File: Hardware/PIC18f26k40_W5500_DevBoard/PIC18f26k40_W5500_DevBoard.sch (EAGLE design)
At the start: 46 parts, among them J2 MAGJACK, J6 USB-B, U1 W5500, U2 PIC18F2523-I/SO

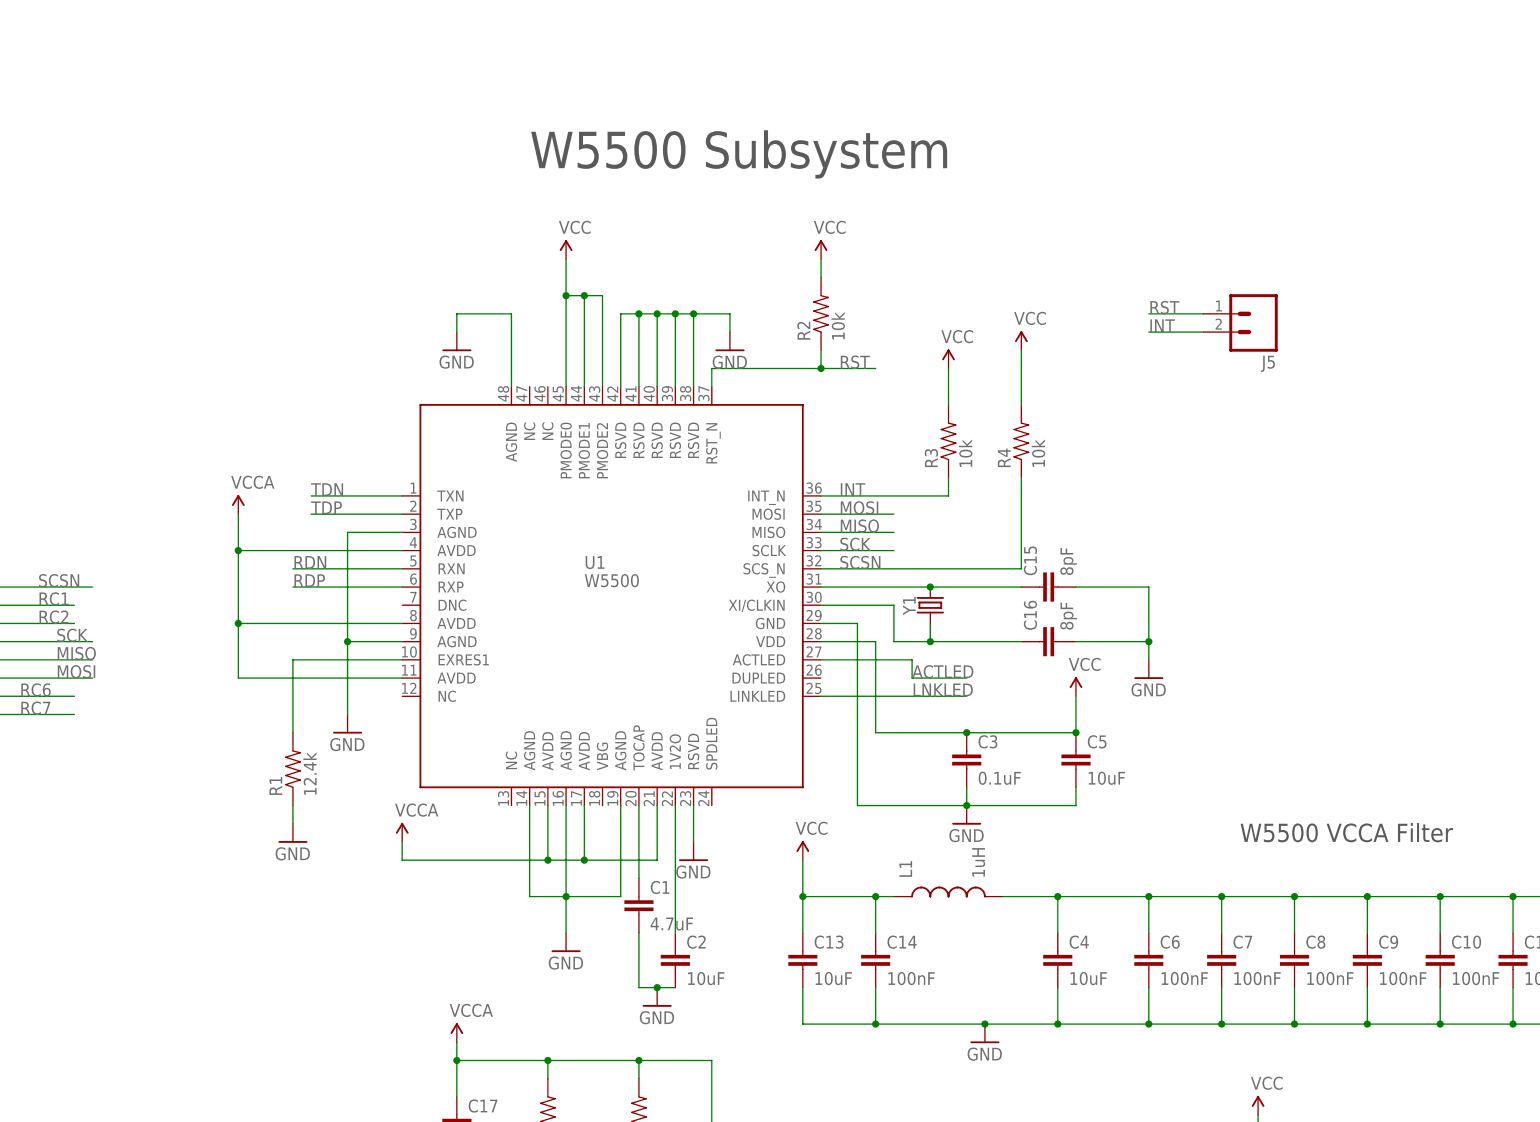
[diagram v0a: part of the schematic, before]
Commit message: #302 Added pull up and pull down resistors to Wiznet direction connections
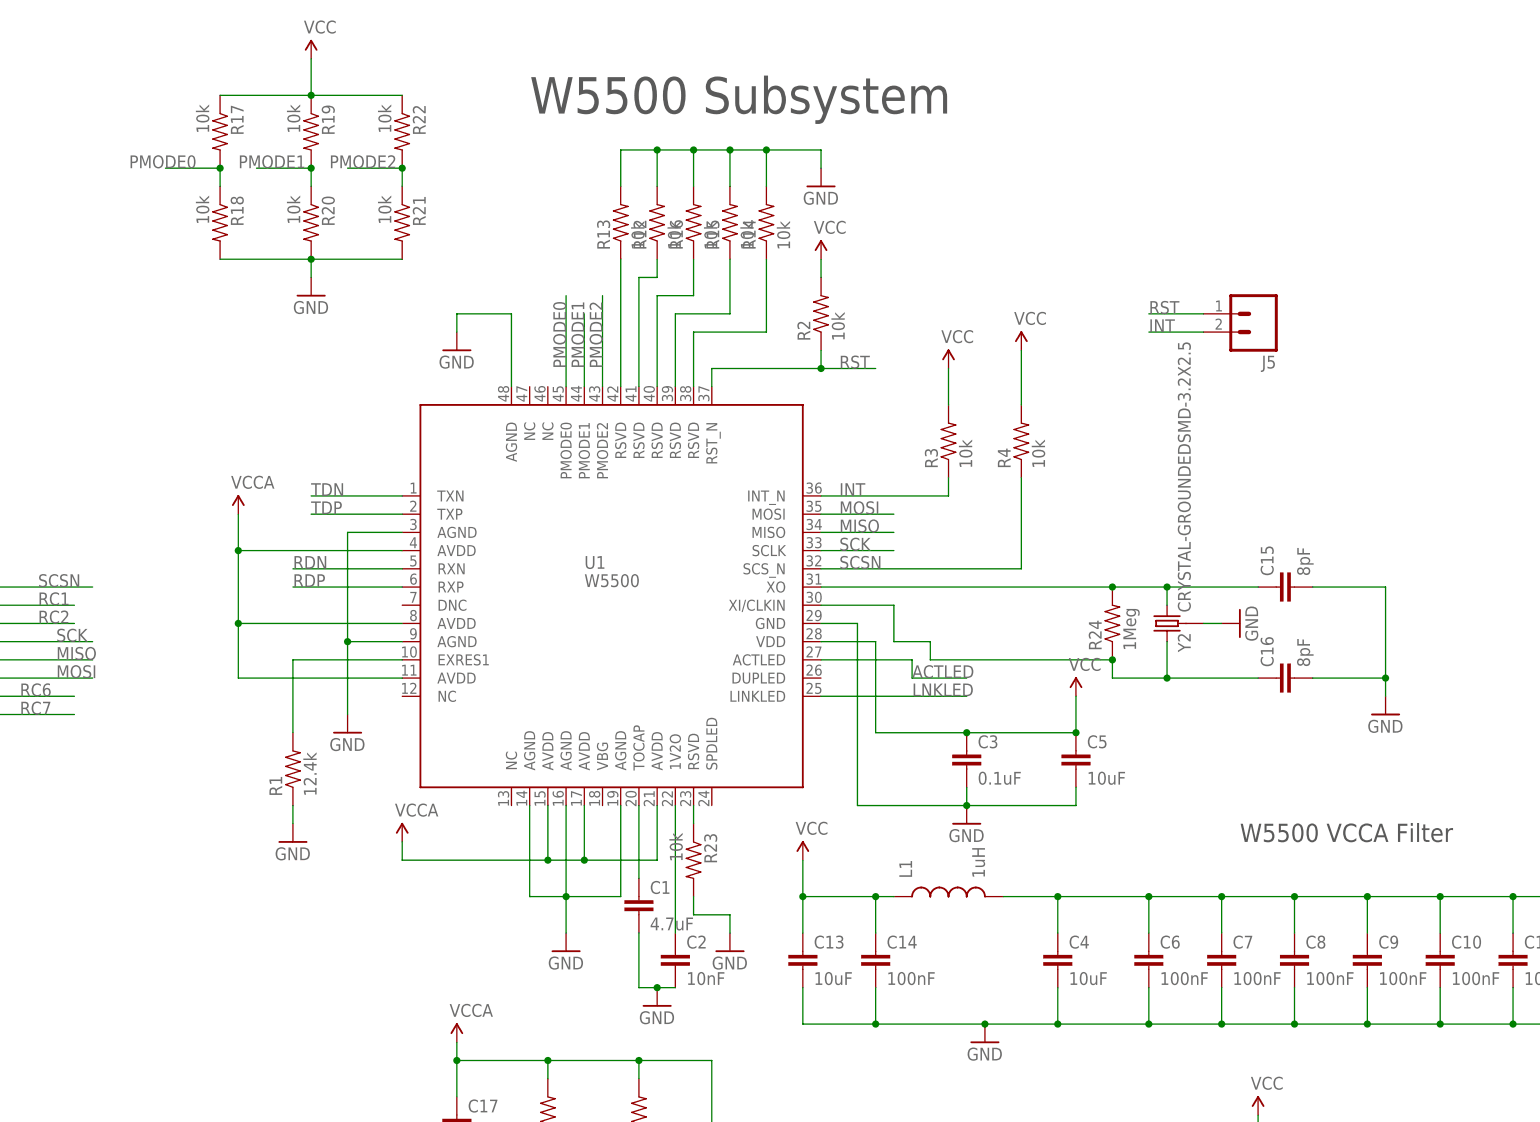
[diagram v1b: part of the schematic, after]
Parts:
- removed Y1: (no value), SparkFun-Clocks:CRYSTALSMD-3.2X2.5
- added R12, R13, R14, R15, R16, R17, R18, R19, R20, R21, R22, R23: 10k, SparkFun-Passives:RESISTOR0603-RES
- added R24: 1Meg, SparkFun-Passives:RESISTOR0603-RES
- added Y2: CRYSTAL-GROUNDEDSMD-3.2X2.5, SparkFun-Clocks:CRYSTAL-GROUNDEDSMD-3.2X2.5
- C2: value 10uF -> 10nF
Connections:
- removed net N$5: C15.1, U1.XO, Y1.2
- new net N$12: R14.1, U1.RSVD@2
- new net N$13: R15.1, U1.RSVD@3
- new net N$14: R16.1, U1.RSVD@4
- new net N$15: R13.1, U1.RSVD@6
- new net N$16: R23.1, U1.RSVD@1
- new net N$17: C16.1, R24.1, U1.XI/CLKIN, Y2.1
- new net N$3: R12.1, U1.RSVD@5
- new net PMODE0: R17.2, R18.1, U1.PMODE0
- new net PMODE1: R19.2, R20.1, U1.PMODE1
- new net PMODE2: R21.1, R22.2, U1.PMODE2
- net GND: now also R12.2, R13.2, R14.2, R15.2, R16.2, R18.2, R20.2, R21.2, R23.2, Y2.3; no longer U1.RSVD@1, U1.RSVD@2, U1.RSVD@3, U1.RSVD@4, U1.RSVD@5, U1.RSVD@6
- net N$6: now also C15.1, R24.2, U1.XO, Y2.2; no longer C16.1, U1.XI/CLKIN, Y1.1
- net VCC: now also R17.1, R19.1, R22.1; no longer U1.PMODE0, U1.PMODE1, U1.PMODE2
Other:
- moved on the sheet: C15, C16
